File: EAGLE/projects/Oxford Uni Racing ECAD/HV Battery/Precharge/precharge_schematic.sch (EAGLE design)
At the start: 59 parts, among them IC1 TLV9001SIDCKR, IC10 74HC1G86GW-Q100H, IC11 74LVC1G32GV,125, IC2 TLV9001SIDCKR, IC3 TLV9001SIDCKR, IC4 TLV9001SIDCKR, IC5 LT1129CS8-3.3#PBF, IC6 LT1129CS8-3.3#PBF, IC7 LT1129CS8-3.3#PBF, IC8 LT1129CS8-3.3#PBF, IC9 74AHC1G08GV,125, J1 T816108A1S102CEU, Q1 BSS138, Q2 BSS138, U1 AMC1350QDWVRQ1AMC1350QDWVRQ1_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, U2 AMC1350QDWVRQ1AMC1350QDWVRQ1_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

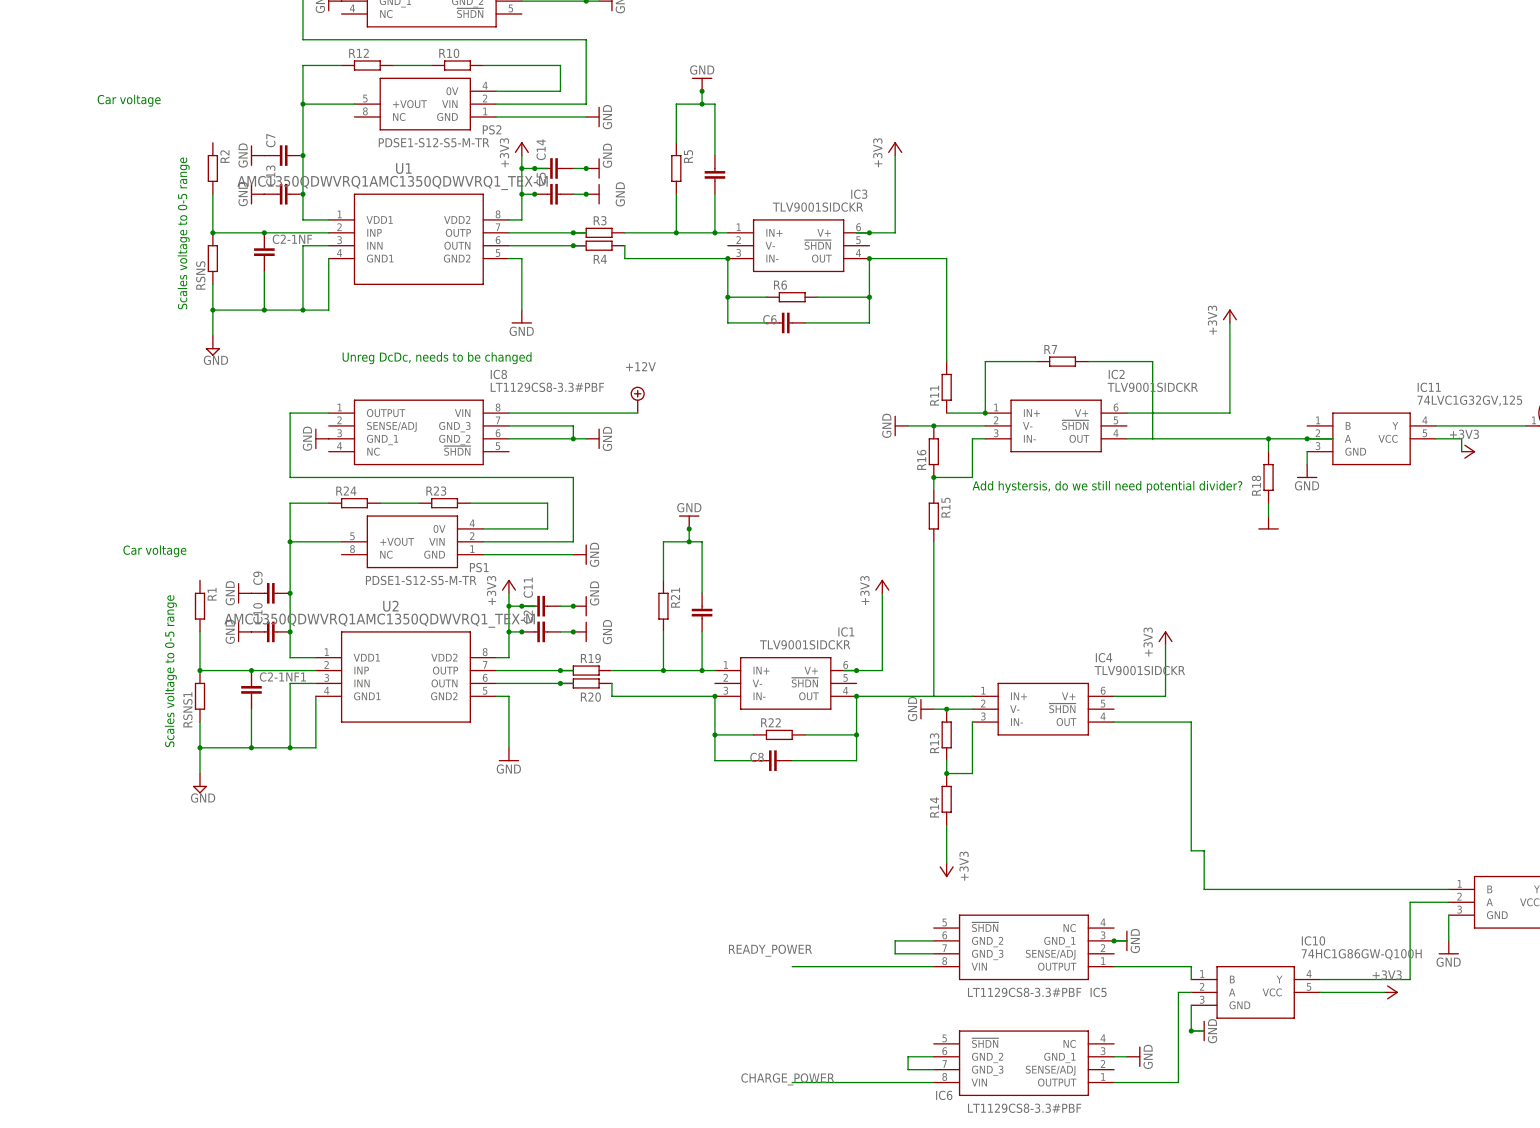
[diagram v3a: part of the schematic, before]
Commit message: first precharge brd deisgn,
need to fix TS/LV separation and add annotation
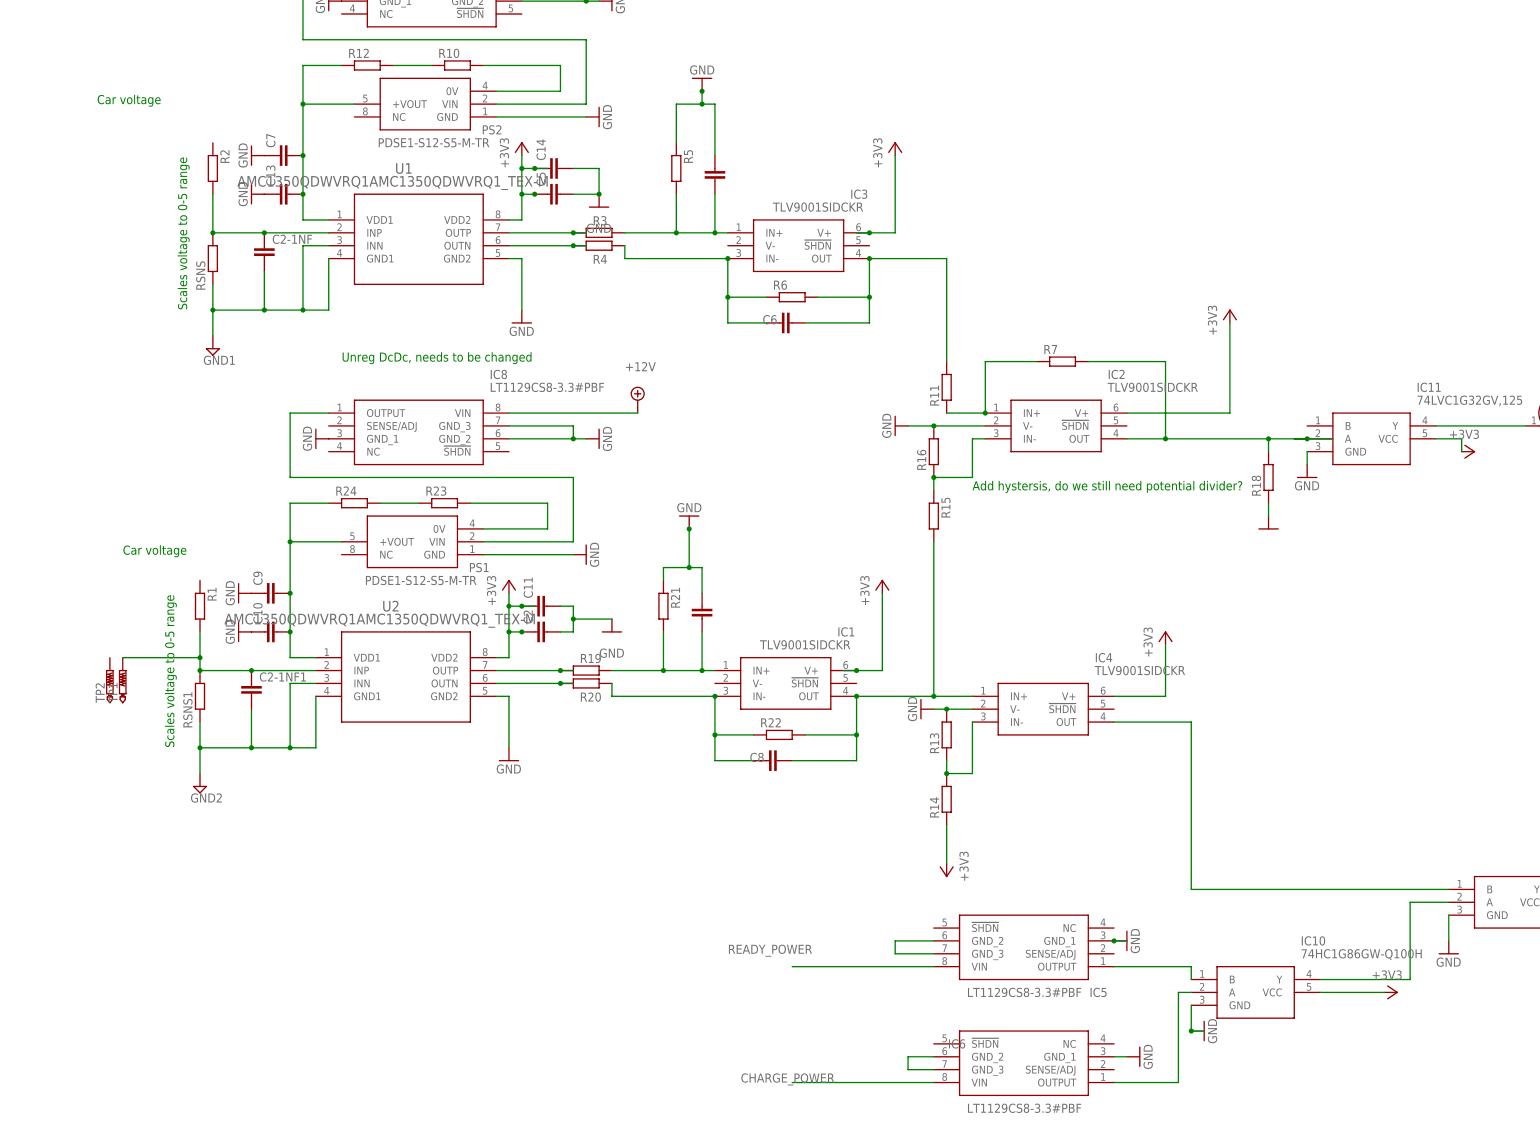
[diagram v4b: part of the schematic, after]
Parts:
- added TP1, TP2: PTR1PAD1-17, testpad:PTR1PAD1-17
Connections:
- removed net N$12: C1.1, R21.1
- removed net N$14: C8.2, IC1.OUT, R22.2
- removed net N$2 (its old number): C3.1, R5.1
- removed net N$20: C14.2
- removed net N$21: C5.2
- removed net N$26: C11.2
- removed net N$27: C2.2
- new net GND1: C2-1NF.2, RSNS.1, U1.GND1, U1.INN
- new net GND2: C2-1NF1.2, RSNS1.1, U2.GND1, U2.INN
- net GND: now also C1.1, C11.2, C14.2, C2.2, C3.1, C5.2, R21.1, R5.1; no longer C2-1NF.2, C2-1NF1.2, RSNS.1, RSNS1.1, U1.GND1, U1.INN, U2.GND1, U2.INN
- net N$16: now also C8.2, IC1.OUT, R22.2
- net N$5: now also TP1.TP

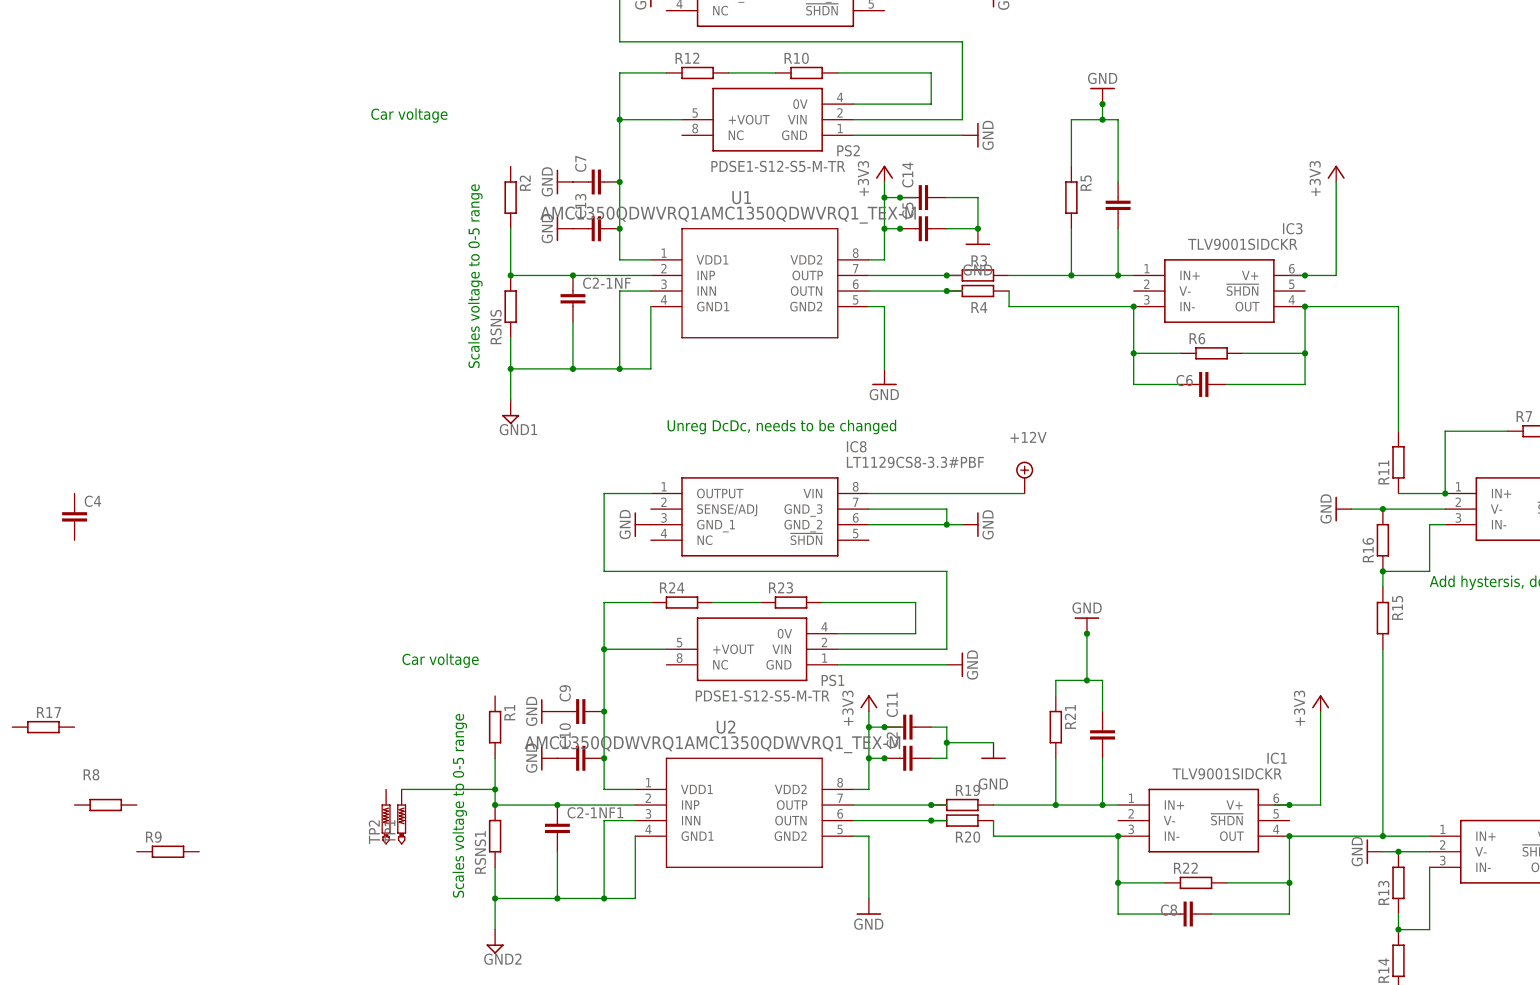
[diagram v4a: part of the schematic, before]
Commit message: Second Precharge board
Fixes the TS-LV separation and changes from 4 layer board to 2 layer board.
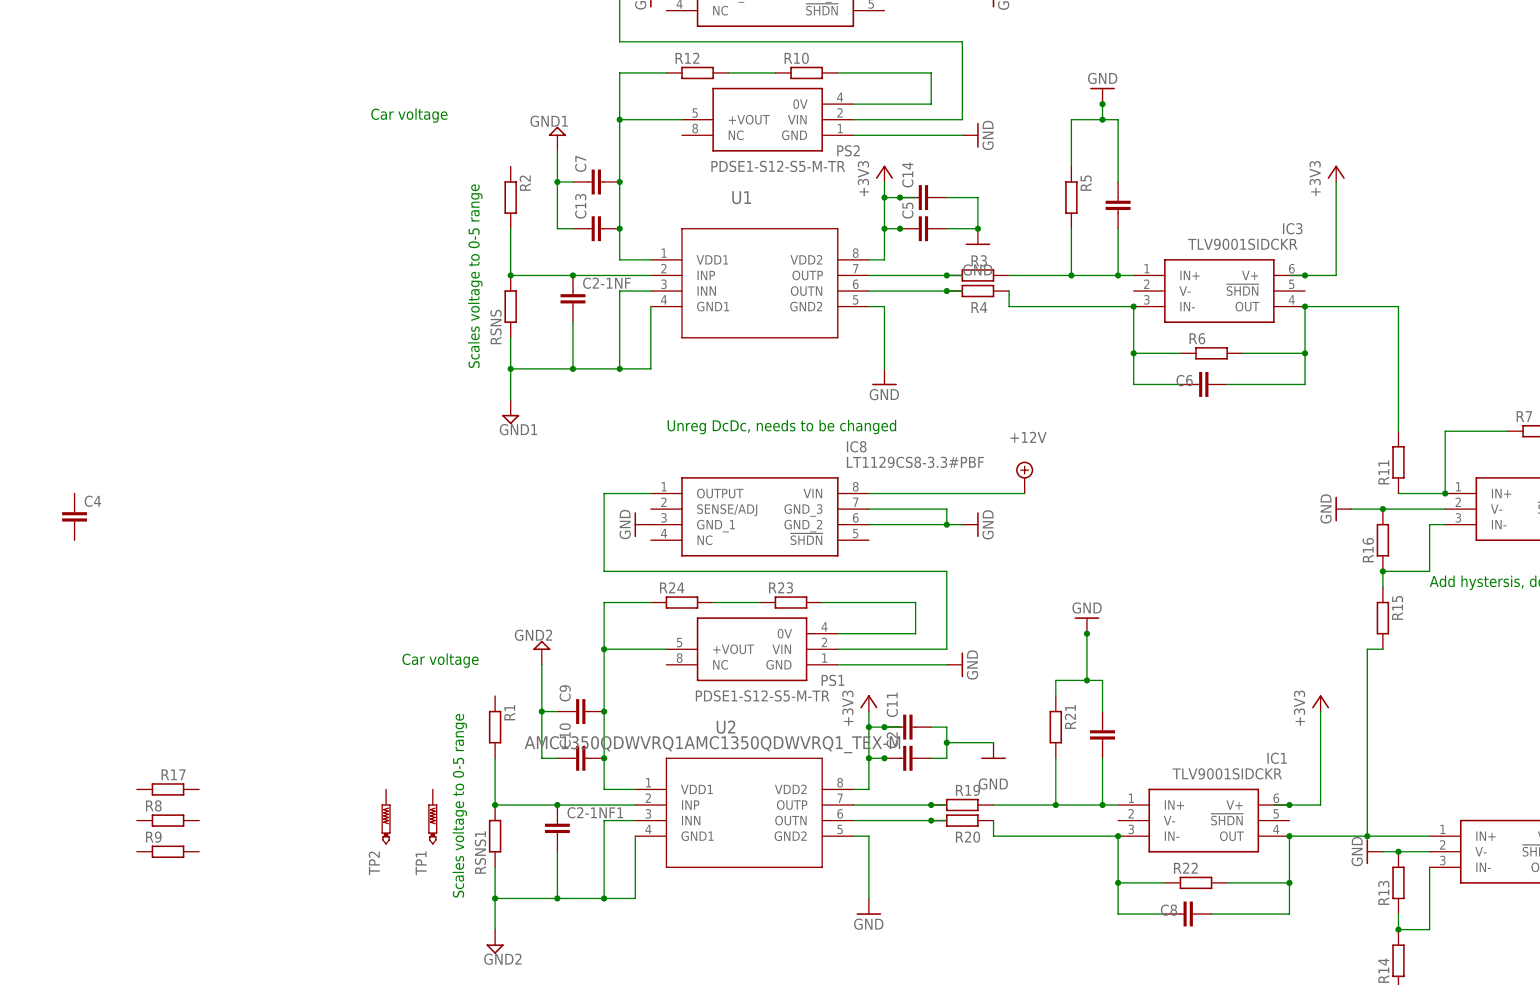
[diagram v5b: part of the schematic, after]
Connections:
- net +3V3 renamed 3V3
- net GND: no longer C10.1, C13.1, C7.1, C9.1
- net GND1: now also C13.1, C7.1
- net GND2: now also C10.1, C9.1
- net N$5: no longer TP1.TP
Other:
- moved on the sheet: R17, R8, TP1

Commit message: Library files + new main board/precharge board 8 pin mini-spox connector
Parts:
- removed IC7: LT1129CS8-3.3#PBF, LT1129CS8-3.3#PBF:LT1129CS8-3.3#PBF
- removed J1: T816108A1S102CEU, T816108A1S102CEU:T816108A1S102CEU
- removed PS2: PDSE1-S12-S5-M-TR, PDSE1-S12-S5-M-TR:PDSE1-S12-S5-M-TR
- removed R10, R12: (no value), rcl:R-EU_R0805
- removed TP1, TP2: PTR1PAD1-17, testpad:PTR1PAD1-17
- added J2, J3, J4, J5: 2-1445098-2, Micro-mate 2-1445098-2:2-1445098-2
- added J6: T816108A1S102CEU, T816108A1S102CEU:T816108A1S102CEU
- PS1: value PDSE1-S12-S5-M-TR -> PDSE1-S12-S12-M-TR; device PDSE1-S12-S5-M-TR:PDSE1-S12-S5-M-TR -> PDSE1-S12-S12-M-TR:PDSE1-S12-S12-M-TR
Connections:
- removed net GND1: C13.1, C2-1NF.2, C7.1, RSNS.1, U1.GND1, U1.INN
- removed net GND2: C10.1, C2-1NF1.2, C9.1, RSNS1.1, U2.GND1, U2.INN
- removed net N$22: C13.2, C7.2, PS2.+VOUT, R12.1, U1.VDD1
- removed net N$23: PS2.0V, R10.2
- removed net N$24: IC7.OUTPUT, PS2.VIN
- removed net N$25: R10.1, R12.2
- removed net N$30: IC8.OUTPUT, PS1.VIN
- removed net N$40: J1.1, Q1.D
- new net GND(LV): C10.1, C13.1, C2-1NF.2, C2-1NF1.2, C7.1, C9.1, PS1.0V, RSNS.1, RSNS1.1, U1.GND1, U1.INN, U2.GND1, U2.INN
- new net N$12: J2.1, J2.2
- new net N$14: J4.1, J4.2
- new net N$15: IC8.GND_1, IC8.SENSE/ADJ
- new net N$20: IC8.VIN, PS1.+VOUT
- new net N$26: IC8.OUTPUT, R23.2
- new net PRECHARGE_DECISION: J6.1, Q1.D
- new net TS+(CAR): J3.1, J3.2, R2.1
- new net TS+(CELLS): J5.1, J5.2, R1.1
- net +12V: now also PS1.VIN; no longer IC7.VIN, IC8.VIN
- net 3V3: now also IC1.!SHDN, IC2.!SHDN, IC3.!SHDN, IC4.!SHDN
- net GND: now also IC8.!SHDN; no longer IC7.GND_1, IC7.GND_2, IC7.GND_3, IC8.GND_1, PS2.GND
- net N$28: no longer PS1.+VOUT
- net N$29: now also C13.2, C7.2, U1.VDD1; no longer PS1.0V, R23.2
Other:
- note added: "Cell (battery) voltage"
- note added: "Connector to main board"
- note added: "Micro Mate voltage inputs"
- note removed: "Unreg DcDc, needs to be changed"

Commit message: main board schematic update with new connectors
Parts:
- removed C4: (no value), rcl:C-EUC0805
- removed J6: T816108A1S102CEU, T816108A1S102CEU:T816108A1S102CEU
- added D1: ES2D, diode:ES2D
- added IC7: LT1129CS8-3.3#PBF, LT1129CS8-3.3#PBF:LT1129CS8-3.3#PBF
- added J1: MINI-SPOX_22035085, Mini-spox_22035085:MINI-SPOX_22035085
- added K2: T9AS1D12-48=T9A, T9AS1D12-12=T9A:T9AS1D12-48=T9A
- added LED1: (no value), led:LEDSML0805
- added PS2: PDSE1-S12-S12-M-TR, PDSE1-S12-S12-M-TR:PDSE1-S12-S12-M-TR
- added R10, R12: (no value), rcl:R-EU_R0805
- added R25: (no value), rcl:R-EU_R0805W
- added R26: (no value), rcl:R-EU_M0805
- R17, R8, R9: device rcl:R-EU_R0805 -> rcl:R-EU_R0805W
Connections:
- new net N$22: R12.1
- new net N$23: IC7.GND_1, IC7.SENSE/ADJ
- new net N$24: IC7.VIN, PS2.+VOUT
- new net N$25: R10.1, R12.2
- new net N$27: IC7.OUTPUT, R10.2
- new net N$30: D1.A, K2.COIL_2, LED1.C, Q2.D
- new net N$31: LED1.A, R26.1
- new net PRECHARGE_EMSDC1: J1.1, K2.NO
- new net PRECHARGE_EMSDC2: J1.2, K2.COM
- net +12V: now also D1.C, IC5.!SHDN, IC6.!SHDN, IC7.!SHDN, IC8.!SHDN, K2.COIL_1, PS2.VIN, R26.2; no longer Q2.D
- net CHARGE_POWER: now also IC11.B
- net GND: now also IC7.GND_2, IC7.GND_3, PS2.GND; no longer IC8.!SHDN
- net GND(LV): now also PS2.0V, R8.1
- net PRECHARGE_DECISION: now also J1.3; no longer J6.1
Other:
- note added: "Sense board"
